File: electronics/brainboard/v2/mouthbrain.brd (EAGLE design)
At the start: 101.6 x 53.3 mm, 28 parts, among them Q1 MOSFET-NCHANNELSMD, Q10 MOSFET-NCHANNELSMD, Q11 MOSFET-NCHANNELSMD, Q12 MOSFET-NCHANNELSMD, Q13 MOSFET-NCHANNELSMD, Q14 MOSFET-NCHANNELSMD, Q15 MOSFET-NCHANNELSMD, Q16 MOSFET-NCHANNELSMD, Q2 MOSFET-NCHANNELSMD, Q3 MOSFET-NCHANNELSMD, Q4 MOSFET-NCHANNELSMD, Q5 MOSFET-NCHANNELSMD, Q6 MOSFET-NCHANNELSMD, Q7 MOSFET-NCHANNELSMD, Q8 MOSFET-NCHANNELSMD, Q9 MOSFET-NCHANNELSMD, U2 ARDUINO-MEGAFULL

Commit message: circuit is ready to rock and roll.
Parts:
- removed JP2: (no value), SparkFun:SCREWTERMINAL-3.5MM-2
- removed U$3, U$4, U$5, U$6: MCP4352, mouthbrain:QFN-20
- added MEGA: ARDUINO-MEGAFULL, SparkFun:ARDUINO_MEGA
- added U$2: FPC-0.5-32, Hoektronics:FPC-PCB-32
- added U1, U3, U4: MCP4352, mouthbrain:QFN-20
- added U5: MOSFET-NCHANNEL-SOIC8, SparkFun:SO08
- U$1: value MOSFET-NCHANNEL-SOIC8 -> DC-DC-CONVERTER; device SparkFun:SO08 -> Hoektronics:DC-DC-MODULE
- U2: value ARDUINO-MEGAFULL -> MCP4352; device SparkFun:ARDUINO_MEGA -> mouthbrain:QFN-20
- moved U2 73.6 mm to (68.6, 29.2)
- moved VDD 44.1 mm to (53.3, 26.7), turned to 90 degrees
- moved Q11 42.4 mm to (67.3, 36.8)
- moved Q12 42.4 mm to (71.1, 36.8)
- moved Q15 42.4 mm to (67.3, 33.0)
- moved Q16 42.4 mm to (71.1, 33.0)
- moved Q3 42.4 mm to (67.3, 44.5)
- moved Q4 42.4 mm to (71.1, 44.5)
- moved Q7 42.4 mm to (67.3, 40.6)
- moved Q8 42.4 mm to (71.1, 40.6)
- moved C1 42.4 mm to (77.5, 27.9)
- moved C2 42.4 mm to (77.5, 24.1)
- moved D1 42.4 mm to (77.5, 31.8)
- moved L1 42.4 mm to (77.5, 43.2)
- moved Q1 42.4 mm to (59.7, 44.5)
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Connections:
- removed net AN0: Q1.1, U2.22
- removed net AN1: Q2.1, U2.23
- removed net AN10: Q11.1, U2.32
- removed net AN11: Q12.1, U2.33
- removed net AN12: Q13.1, U2.34
- removed net AN13: Q14.1, U2.35
- removed net AN14: Q15.1, U2.36
- removed net AN15: Q16.1
- removed net AN2: Q3.1, U2.24
- removed net AN3: Q4.1, U2.25
- removed net AN4: Q5.1, U2.26
- removed net AN5: Q6.1, U2.27
- removed net AN6: Q7.1, U2.28
- removed net AN7: Q8.1, U2.29
- removed net AN8: Q9.1, U2.30
- removed net AN9: Q10.1, U2.31
- removed net ANODE0: Q1.3
- removed net ANODE1: Q2.3
- removed net ANODE10: Q11.3
- removed net ANODE11: Q12.3
- removed net ANODE12: Q13.3
- removed net ANODE13: Q14.3
- removed net ANODE14: Q15.3
- removed net ANODE15: Q16.3
- removed net ANODE2: Q3.3
- removed net ANODE3: Q4.3
- removed net ANODE4: Q5.3
- removed net ANODE5: Q6.3
- removed net ANODE6: Q7.3
- removed net ANODE7: Q8.3
- removed net ANODE8: Q9.3
- removed net ANODE9: Q10.3
- removed net N$3: C1.1, D1.C
- removed net OUT0: U$3.10, U2.A0
- removed net OUT1: U$3.7, U2.A1
- removed net OUT10: U$5.17, U2.A10
- removed net OUT11: U$5.20, U2.A11
- removed net OUT12: U$6.10, U2.A12
- removed net OUT13: U$6.7, U2.A13
- removed net OUT14: U$6.17, U2.A14
- removed net OUT15: U$6.20, U2.A15
- removed net OUT2: U$3.17, U2.A2
- removed net OUT3: U$3.20, U2.A3
- removed net OUT4: U$4.10, U2.A4
- removed net OUT5: U$4.7, U2.A5
- removed net OUT6: U$4.17, U2.A6
- removed net OUT7: U$4.20, U2.A7
- removed net OUT8: U$5.10, U2.A8
- removed net OUT9: U$5.7, U2.A9
- new net AOUT0: MEGA.A0, U$2.P$2, U1.10
- new net AOUT1: MEGA.A1, U$2.P$4, U1.7
- new net AOUT10: MEGA.A10, U$2.P$22, U3.17
- new net AOUT11: MEGA.A11, U$2.P$24, U3.20
- new net AOUT12: MEGA.A12, U$2.P$26, U4.10
- new net AOUT13: MEGA.A13, U$2.P$28, U4.7
- new net AOUT14: MEGA.A14, U$2.P$30, U4.17
- new net AOUT15: MEGA.A15, U$2.P$32, U4.20
- new net AOUT2: MEGA.A2, U$2.P$6, U1.17
- new net AOUT3: MEGA.A3, U$2.P$8, U1.20
- new net AOUT4: MEGA.A4, U$2.P$10, U2.10
- new net AOUT5: MEGA.A5, U$2.P$12, U2.7
- new net AOUT6: MEGA.A6, U$2.P$14, U2.17
- new net AOUT7: MEGA.A7, U$2.P$16, U2.20
- new net AOUT8: MEGA.A8, U$2.P$18, U3.10
- new net AOUT9: MEGA.A9, U3.7
- new net CIN0: MEGA.22, Q1.1
- new net CIN1: MEGA.23, Q2.1
- new net CIN10: MEGA.32, Q11.1
- new net CIN11: MEGA.33, Q12.1
- new net CIN12: MEGA.34, Q13.1
- new net CIN13: MEGA.35, Q14.1
- new net CIN14: MEGA.36, Q15.1
- new net CIN15: MEGA.37, Q16.1
- new net CIN2: MEGA.24, Q3.1
- new net CIN3: MEGA.25, Q4.1
- new net CIN4: MEGA.26, Q5.1
- new net CIN5: MEGA.27, Q6.1
- new net CIN6: MEGA.28, Q7.1
- new net CIN7: MEGA.29, Q8.1
- new net CIN8: MEGA.30, Q9.1
- new net CIN9: MEGA.31, Q10.1
- new net COUT0: Q1.3, U$2.P$1
- new net COUT1: Q2.3, U$2.P$3
- new net COUT10: Q11.3, U$2.P$21
- new net COUT11: Q12.3, U$2.P$23
- new net COUT12: Q13.3, U$2.P$25
- new net COUT13: Q14.3, U$2.P$27
- new net COUT14: Q15.3, U$2.P$29
- new net COUT15: Q16.3, U$2.P$31
- new net COUT2: Q3.3, U$2.P$5
- new net COUT3: Q4.3, U$2.P$7
- new net COUT4: Q5.3, U$2.P$9
- new net COUT5: Q6.3, U$2.P$11
- new net COUT6: Q7.3, U$2.P$13
- new net COUT7: Q8.3, U$2.P$15
- new net COUT8: Q9.3, U$2.P$17
- new net COUT9: Q10.3, U$2.P$19, U$2.P$20
- net !CS1: now also MEGA.6, U1.2; no longer U$3.2, U2.6
- net !CS2: now also MEGA.7, U2.2; no longer U$4.2, U2.7
- net !CS3: now also MEGA.8, U3.2; no longer U$5.2, U2.8
- net !CS4: now also MEGA.9, U4.2; no longer U$6.2, U2.9
- net !RESET: now also MEGA.2, U1.13, U2.13, U3.13, U4.13; no longer U$3.13, U$4.13, U$5.13, U$6.13, U2.2
- net BOOST: now also C1.1, D1.C
- net BOOST_FET: now also MEGA.11, U5.4; no longer U$1.4
- net EXT: now also U$1.OUT+; no longer JP2.1
- net GND: now also MEGA.GND@0, MEGA.GND@1, MEGA.GND@2, MEGA.GND@3, MEGA.GND@4, U$1.IN-, U$1.OUT-, U1.1, U1.11, U1.16, U1.5, U1.6, U2.1, U2.11, U2.16, U2.5, U2.6, U3.1, U3.11, U3.16, U3.5, U3.6, U4.1, U4.11, U4.16, U4.5, U4.6, U5.5, U5.6, U5.7, U5.8; no longer JP2.2, U$1.5, U$1.6, U$1.7, U$1.8, U$3.5, U$4.5, U$5.5, U$6.5, U2.GND@0, U2.GND@1, U2.GND@2, U2.GND@3, U2.GND@4
- net N$1: now also U5.1, U5.2, U5.3; no longer U$1.1, U$1.2, U$1.3
- net SCK: now also MEGA.3, U1.3, U3.3, U4.3; no longer U$3.3, U$4.3, U$5.3, U$6.3
- net SI: now also MEGA.4, U1.4, U3.4, U4.4; no longer U$3.4, U$4.4, U$5.4, U$6.4
- net SO: now also MEGA.5; no longer U2.5
- net VCC: now also U$1.IN+, U1.15, U2.15, U3.15, U4.15; no longer U$3.15, U$4.15, U$5.15, U$6.15
- net VDD: now also U1.18, U1.19, U1.8, U1.9, U2.18, U2.19, U2.8, U2.9, U3.18, U3.19, U3.8, U3.9, U4.18, U4.19, U4.8, U4.9; no longer U$3.18, U$3.19, U$3.8, U$3.9, U$4.18, U$4.19, U$4.8, U$4.9, U$5.18, U$5.19, U$5.8, U$5.9, U$6.18, U$6.19, U$6.8, U$6.9

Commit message: routed the brainboard
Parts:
- moved Q1 21.6 mm to (59.7, 22.9), turned to 90 degrees
- moved U3 20.4 mm to (82.5, 25.4), turned to 90 degrees
- moved C2 19.7 mm to (82.5, 43.2), turned to 270 degrees
- moved Q2 18.2 mm to (59.7, 26.7), turned to 90 degrees
- moved Q5 18.2 mm to (63.5, 22.9), turned to 90 degrees
- moved U4 17.3 mm to (82.5, 34.3), turned to 90 degrees
- moved L1 16.5 mm to (61.0, 43.2), turned to 270 degrees
- moved VDD 16.5 mm to (53.3, 43.2)
- moved Q3 15.9 mm to (59.7, 30.5), turned to 90 degrees
- moved Q9 15.9 mm to (67.3, 22.9), turned to 90 degrees
- moved Q13 15.3 mm to (71.1, 22.9), turned to 90 degrees
- moved Q4 15.3 mm to (59.7, 34.3), turned to 90 degrees
- moved C1 15.2 mm to (77.5, 43.2), turned to 270 degrees
- moved U1 14.5 mm to (76.2, 25.4), turned to 90 degrees
- moved Q6 14.0 mm to (63.5, 26.7), turned to 90 degrees
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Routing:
- net GND: track 0.00 -> 308.3 mm, vias 0 -> 8
- net VCC: track 0.00 -> 124.3 mm, vias 0 -> 8
- net CIN4: track 0.00 -> 99.7 mm, vias 0 -> 2
- net CIN10: track 0.00 -> 98.5 mm, vias 0 -> 7
- net VDD: track 0.00 -> 84.4 mm, vias 0 -> 8
- net CIN1: track 0.00 -> 83.2 mm, vias 0 -> 3
- net AOUT4: track 0.00 -> 79.7 mm, vias 0 -> 2
- net !CS3: track 0.00 -> 78.7 mm, vias 0 -> 4
- net SI: track 0.00 -> 78.5 mm, vias 0 -> 10
- net CIN5: track 0.00 -> 78.3 mm, vias 0 -> 1
- net AOUT5: track 0.00 -> 77.5 mm, vias 0 -> 2
- net CIN9: track 0.00 -> 76.5 mm, vias 0 -> 5
- net CIN12: track 0.00 -> 71.6 mm, vias 0 -> 2
- net AOUT6: track 0.00 -> 67.1 mm, vias 0 -> 5
- net SCK: track 0.00 -> 66.6 mm, vias 0 -> 7
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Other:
- board text removed: "GND"
- board text removed: "V+"

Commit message: latest routing
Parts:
- moved U$1 0.18 mm to (32.9, 29.1)
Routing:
- net GND: track 308.3 -> 310.7 mm
- net VCC: track 124.3 -> 126.7 mm

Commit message: routed a bunch of the brainboard.
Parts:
- removed MEGA: ARDUINO-MEGAFULL, SparkFun:ARDUINO_MEGA
- added U$3: ARDUINO-MEGA, Hoektronics:ARDUINO-MEGA
- U$2: value FPC-0.5-32 -> FPC-0.5-32HORIZ; device Hoektronics:FPC-PCB-32 -> Hoektronics:FPC-32-HORIZONTAL
- moved C2 48.5 mm to (48.3, 8.89), turned to 180 degrees
- moved C1 41.3 mm to (48.3, 14.0), turned to 180 degrees
- moved Q2 37.7 mm to (91.4, 47.0), turned to 0 degrees
- moved Q1 37.4 mm to (88.3, 47.0), turned to 0 degrees
- moved D1 35.9 mm to (48.3, 17.8), turned to 0 degrees
- moved Q4 32.7 mm to (91.4, 41.9), turned to 0 degrees
- moved Q3 30.8 mm to (88.3, 41.9), turned to 0 degrees
- moved Q16 30.6 mm to (91.4, 11.4), turned to 0 degrees
- moved Q6 29.7 mm to (91.4, 36.8), turned to 0 degrees
- moved Q5 28.4 mm to (88.3, 36.8), turned to 0 degrees
- moved Q8 28.1 mm to (91.4, 31.8), turned to 0 degrees
- moved Q12 27.3 mm to (91.4, 21.6), turned to 0 degrees
- moved U5 26.9 mm to (48.3, 24.1), turned to 270 degrees
- moved Q15 25.6 mm to (88.3, 11.4), turned to 0 degrees
- moved Q7 24.8 mm to (88.3, 31.8), turned to 0 degrees
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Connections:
- net !CS1: now also U$3.D6; no longer MEGA.6
- net !CS2: now also U$3.D5; no longer MEGA.7
- net !CS3: now also U$3.D4; no longer MEGA.8
- net !CS4: now also U$3.D3; no longer MEGA.9
- net !RESET: now also U$3.D2; no longer MEGA.2
- net AOUT0: now also U$3.A0, U1.7; no longer MEGA.A0, U1.10
- net AOUT1: now also U$3.A1, U1.10; no longer MEGA.A1, U1.7
- net AOUT10: now also U$3.A10; no longer MEGA.A10
- net AOUT11: now also U$3.A11; no longer MEGA.A11
- net AOUT12: now also U$3.A12, U4.7; no longer MEGA.A12, U4.10
- net AOUT13: now also U$3.A13, U4.10; no longer MEGA.A13, U4.7
- net AOUT14: now also U$3.A14; no longer MEGA.A14
- net AOUT15: now also U$3.A15; no longer MEGA.A15
- net AOUT2: now also U$3.A2; no longer MEGA.A2
- net AOUT3: now also U$3.A3; no longer MEGA.A3
- net AOUT4: now also U$3.A4, U2.7; no longer MEGA.A4, U2.10
- net AOUT5: now also U$3.A5, U2.10; no longer MEGA.A5, U2.7
- net AOUT6: now also U$3.A6; no longer MEGA.A6
- net AOUT7: now also U$3.A7; no longer MEGA.A7
- net AOUT8: now also U$3.A8, U3.7; no longer MEGA.A8, U3.10
- net AOUT9: now also U$2.P$20, U$3.A9, U3.10; no longer MEGA.A9, U3.7
- net BOOST_FET: now also U$3.D11; no longer MEGA.11
- net CIN0: now also U$3.D22; no longer MEGA.22
- net CIN1: now also U$3.D24; no longer MEGA.23
- net CIN10: now also U$3.D42; no longer MEGA.32
- net CIN11: now also U$3.D44; no longer MEGA.33
- net CIN12: now also U$3.D46; no longer MEGA.34
- net CIN13: now also U$3.D48; no longer MEGA.35
- net CIN14: now also U$3.D50; no longer MEGA.36
- net CIN15: now also U$3.D52; no longer MEGA.37
- net CIN2: now also U$3.D26; no longer MEGA.24
- net CIN3: now also U$3.D28; no longer MEGA.25
- net CIN4: now also U$3.D30; no longer MEGA.26
- net CIN5: now also U$3.D32; no longer MEGA.27
- net CIN6: now also U$3.D34; no longer MEGA.28
- net CIN7: now also U$3.D36; no longer MEGA.29
- net CIN8: now also U$3.D38; no longer MEGA.30
- net CIN9: now also U$3.D40; no longer MEGA.31
- net COUT9: no longer U$2.P$20
- net GND: now also U$3.GND4, U$3.GND5; no longer MEGA.GND@0, MEGA.GND@1, MEGA.GND@2, MEGA.GND@3, MEGA.GND@4
- net SCK: now also U$3.D7; no longer MEGA.3
- net SI: now also U$3.D8; no longer MEGA.4
- net SO: now also U$3.D9; no longer MEGA.5
- net VCC: now also U$3.5V-3
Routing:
- net GND: track 310.7 -> 81.6 mm, vias 8 -> 0
- net CIN4: track 99.7 -> 7.61 mm, vias 2 -> 0
- net CIN10: track 98.5 -> 7.61 mm, vias 7 -> 0
- net VDD: track 84.4 -> 5.08 mm, vias 8 -> 0
- net CIN1: track 83.2 -> 4.40 mm, vias 3 -> 0
- net !CS3: track 78.7 -> 0.00 mm, vias 4 -> 0
- net SI: track 78.5 -> 0.00 mm, vias 10 -> 0
- net VCC: track 126.7 -> 50.4 mm, vias 8 -> 1
- net CIN5: track 78.3 -> 4.33 mm, vias 1 -> 0
- net CIN9: track 76.5 -> 4.33 mm, vias 5 -> 0
- net SCK: track 66.6 -> 0.00 mm, vias 7 -> 0
- net COUT11: track 64.3 -> 0.00 mm, vias 4 -> 0
- net !CS4: track 64.0 -> 0.00 mm, vias 5 -> 0
- net CIN12: track 71.6 -> 7.61 mm, vias 2 -> 0
- net !CS1: track 63.7 -> 0.00 mm, vias 6 -> 0
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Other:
- board outline removed

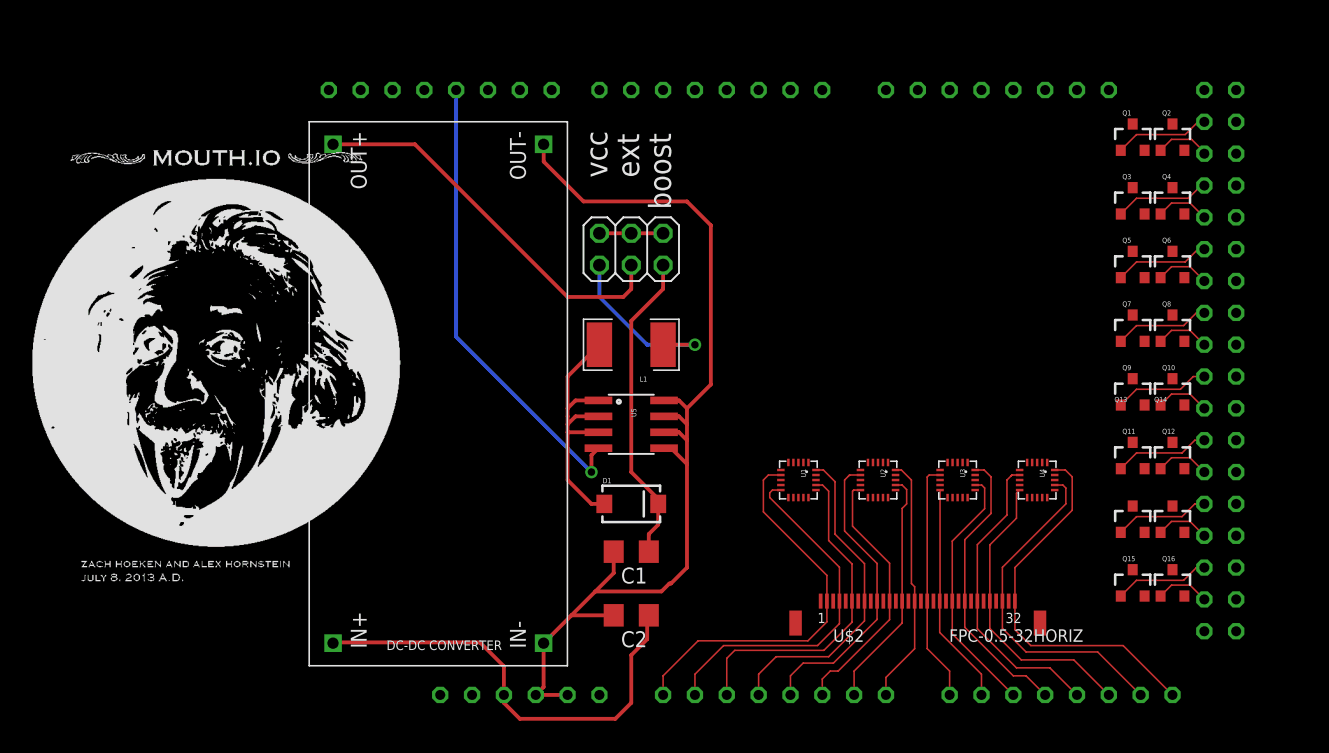
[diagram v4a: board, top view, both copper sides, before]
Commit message: layout mods to the brainboard.
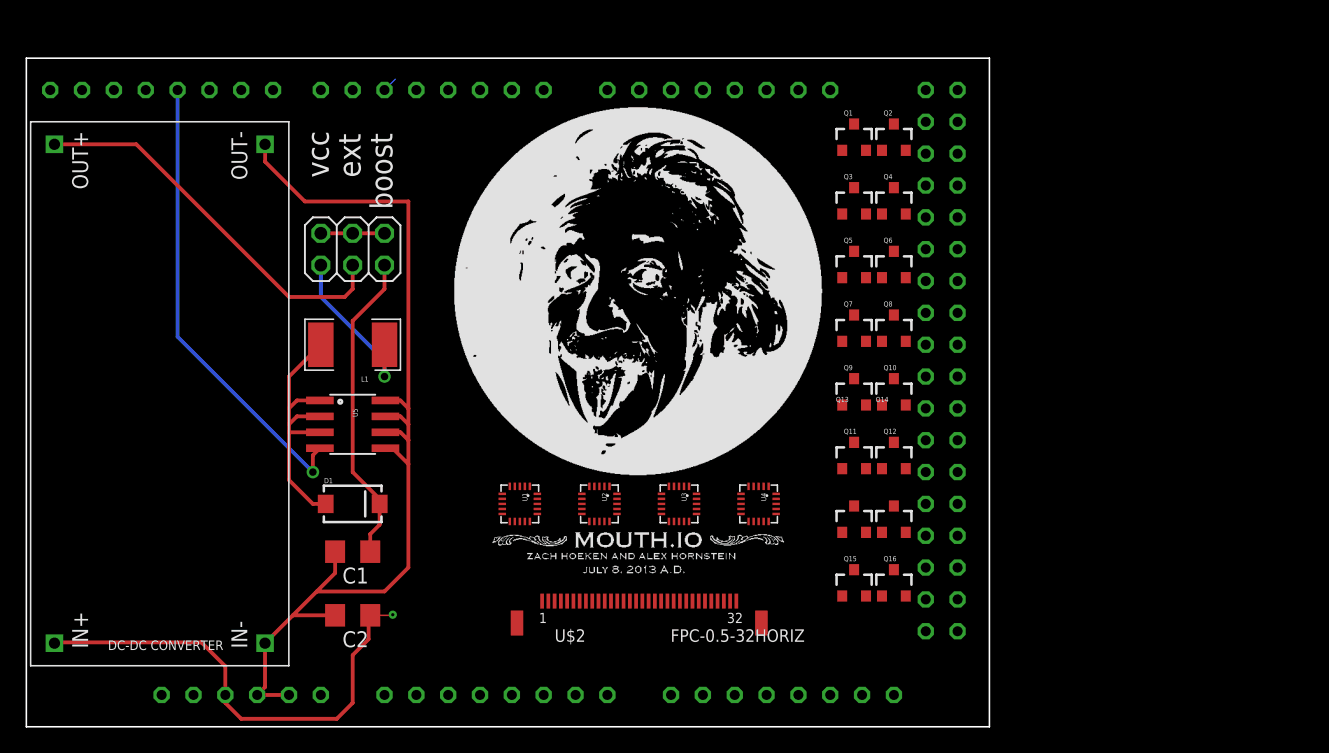
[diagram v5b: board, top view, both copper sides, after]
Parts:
- moved U1 22.3 mm to (39.4, 17.8)
- moved U3 22.3 mm to (52.1, 17.8)
- moved U2 22.3 mm to (45.7, 17.8)
- moved U4 22.3 mm to (58.4, 17.8)
- moved U$1 22.2 mm to (10.6, 26.6)
- moved U$2 22.2 mm to (48.9, 9.53)
- moved U$3 22.2 mm to (-22.2, 0.00)
- moved C1 22.2 mm to (26.0, 14.0)
- moved C2 22.2 mm to (26.0, 8.89)
- moved D1 22.2 mm to (26.0, 17.8)
- moved L1 22.2 mm to (26.0, 30.5)
- moved U5 22.2 mm to (26.0, 24.1)
- moved VDD 22.2 mm to (26.0, 38.1)
- moved Q1 22.2 mm to (66.0, 47.0)
- moved Q10 22.2 mm to (69.2, 26.7)
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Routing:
- net AOUT0: track 31.4 -> 0.00 mm
- net AOUT15: track 30.4 -> 0.00 mm
- net AOUT1: track 28.6 -> 0.00 mm
- net AOUT14: track 27.5 -> 0.00 mm
- net AOUT2: track 26.5 -> 0.00 mm
- net AOUT3: track 25.9 -> 0.00 mm
- net AOUT12: track 24.2 -> 0.00 mm
- net AOUT4: track 23.9 -> 0.00 mm
- net AOUT13: track 23.7 -> 0.00 mm
- net AOUT11: track 23.0 -> 0.00 mm
- net AOUT5: track 20.7 -> 0.00 mm
- net AOUT10: track 20.5 -> 0.00 mm
- net AOUT7: track 19.8 -> 0.00 mm
- net AOUT8: track 19.2 -> 0.00 mm
- net AOUT6: track 19.2 -> 0.00 mm
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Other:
- board outline added: 76.8 x 53.3 mm
